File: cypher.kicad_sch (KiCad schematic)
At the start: 32 parts, among them J3 Breakout, Q1 BC850, Q2 MMBT3904, SW1 SW_Push, U1 STM32F072CBTx, U2 USBLC6-2P6, U3 LD3985G33R_TSOT23

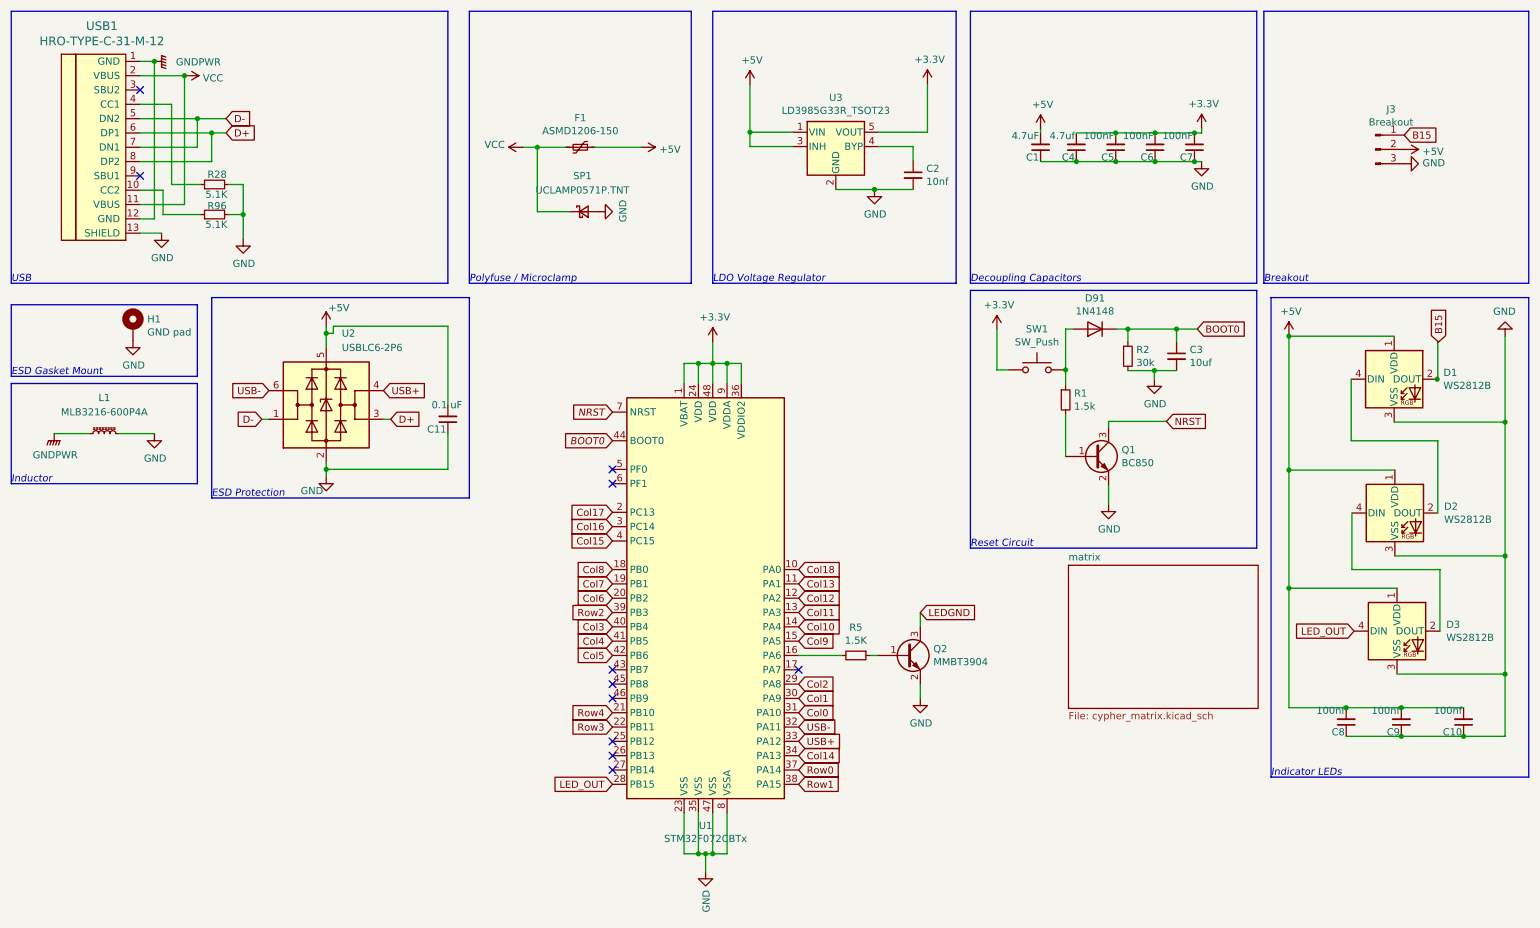
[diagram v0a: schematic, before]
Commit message: updates ESD and reset circuit
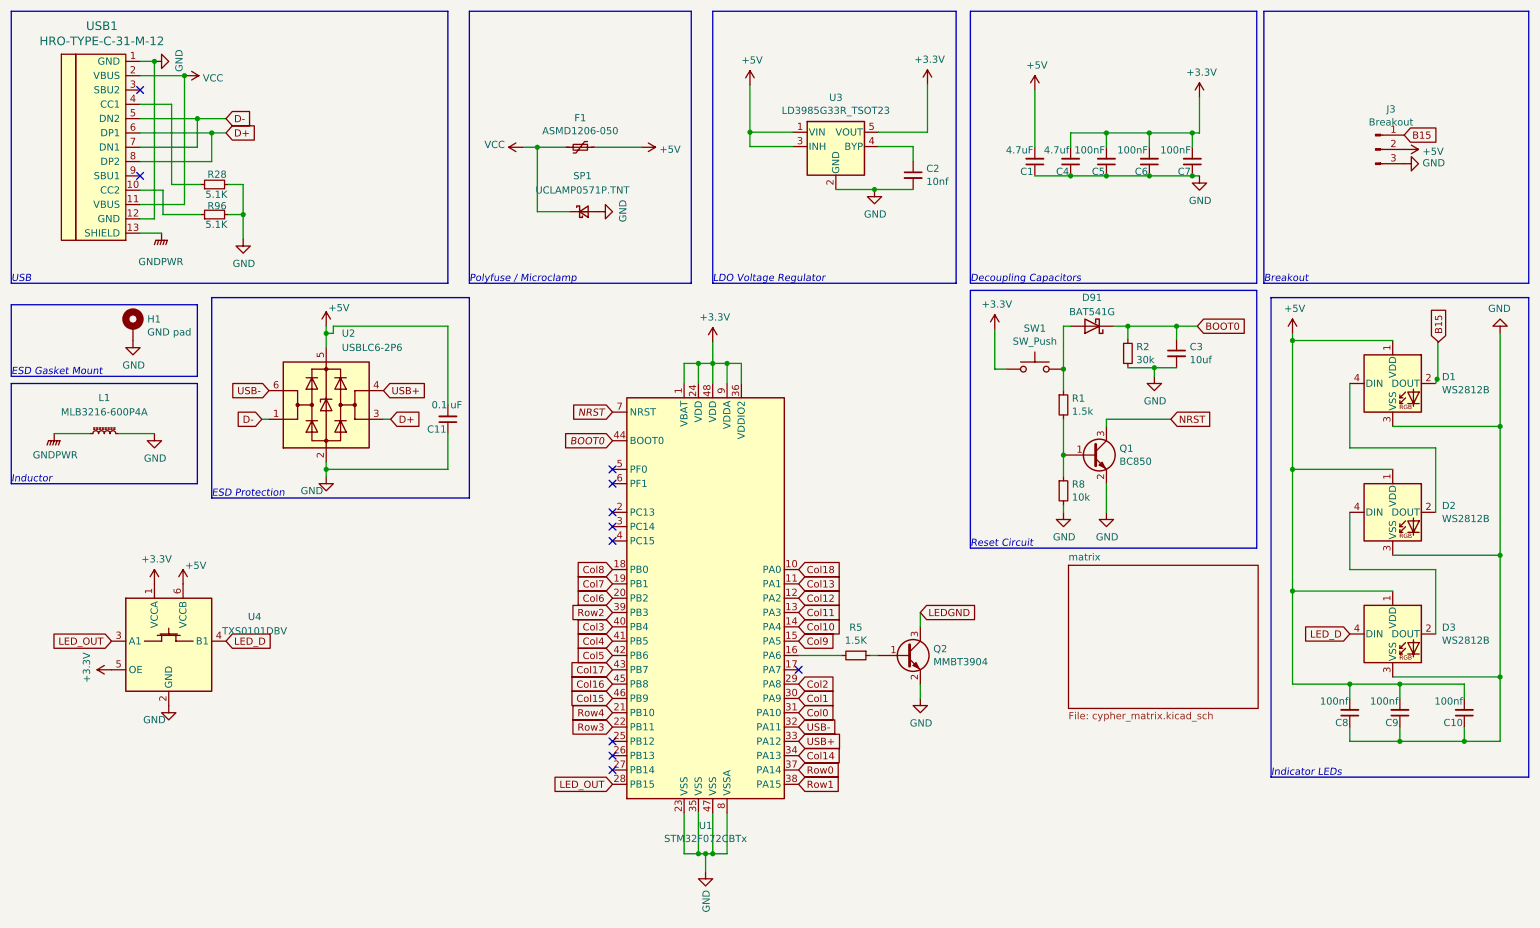
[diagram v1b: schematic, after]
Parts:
- removed D91: 1N4148, Diode_SMD:D_SOD-123, symbol Device:D
- added D91: BAT541G, Diode_SMD:D_SOD-123, symbol Device:D_Schottky
- added R8: 10k, Resistor_SMD:R_0603_1608Metric, symbol Device:R_Small
- added U4: TXS0101DBV, Package_TO_SOT_SMD:SOT-23-6, symbol random-keyboard-parts:TXS0101DBV
- F1: value ASMD1206-150 -> ASMD1206-050
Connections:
- net +3.3V: now also U4.1 (VCCA), U4.5 (OE)
- net +5V: now also U4.6 (VCCB)
- net BOOT0: now also D91.1 (K)
- net Col15: now also U1.46 (PB9); no longer U1.4 (PC15)
- net Col16: now also U1.45 (PB8); no longer U1.3 (PC14)
- net Col17: now also U1.43 (PB7); no longer U1.2 (PC13)
- net GND: now also USB1.1 (GND), USB1.12 (GND), R8.2, U4.2 (GND); no longer USB1.13 (SHIELD)
- net GNDPWR: now also USB1.13 (SHIELD); no longer USB1.1 (GND), USB1.12 (GND)
- net LED_OUT: now also U4.3 (A1); no longer D3.4 (DIN)
- net at Q1.1 (B), R1.2: now also R8.1
- net at R1.1, SW1.2: now also D91.2 (A)
- new net LED_D: D3.4 (DIN), U4.4 (B1)
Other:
- moved on the sheet: C1, C10, C3, C4, C5, C6, C7, C8, C9, D1, D3, R1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

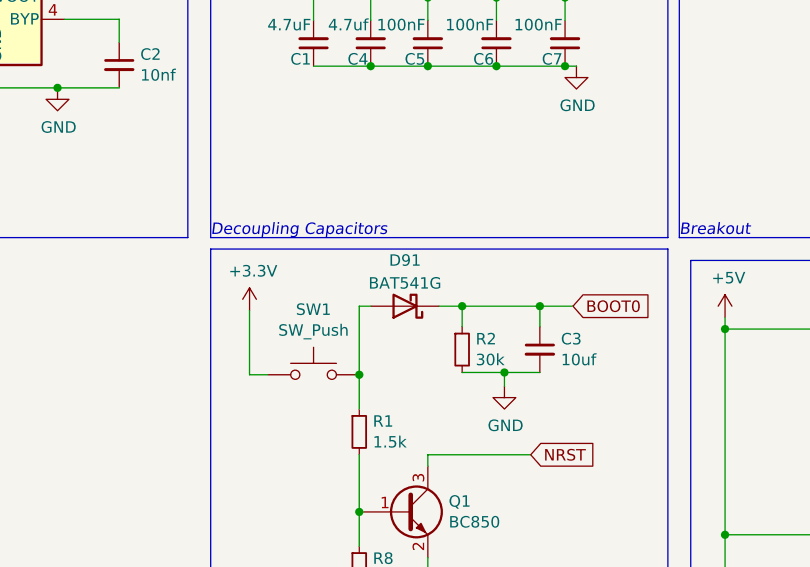
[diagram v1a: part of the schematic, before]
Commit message: Updated incorrect part no
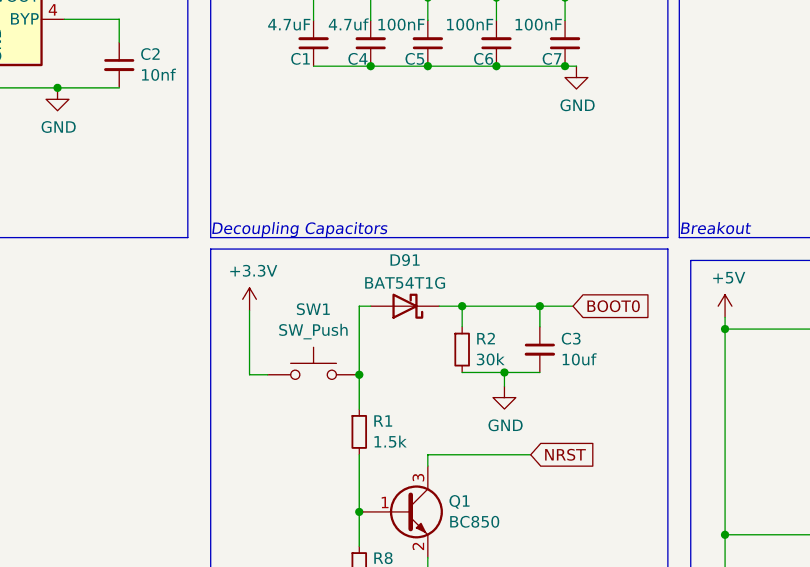
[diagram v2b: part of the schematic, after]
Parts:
- D91: value BAT541G -> BAT54T1G
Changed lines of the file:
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@@
     (in_bom yes) (on_board yes)
     (property "Reference" "D91" (id 0) (at 205.74 66.04 0))
-    (property "Value" "BAT541G" (id 1) (at 205.74 68.58 0))
+    (property "Value" "BAT54T1G" (id 1) (at 205.74 68.58 0))
     (property "Footprint" "Diode_SMD:D_SOD-123" (id 2) (at 205.74 71.12 0)
       (effects (font (size 1.27 1.27)) hide)
@@
     )
     (path "/a76d12c0-1c07-4d80-89aa-54a0de2bbfc3"
-      (reference "D91") (unit 1) (value "BAT541G") (footprint "Diode_SMD:D_SOD-123")
+      (reference "D91") (unit 1) (value "BAT54T1G") (footprint "Diode_SMD:D_SOD-123")
     )
     (path "/00000000-0000-0000-0000-00005c1aa6cb/00000000-0000-0000-0000-00005e7d8bb8"
